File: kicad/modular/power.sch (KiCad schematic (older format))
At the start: 25 parts

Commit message: removed signal shield from power module, updated page settings
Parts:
- removed J?: SignalShield, symbol Connector_Shield:Shield_2x1x6
- J?: value PowerShield -> POWER
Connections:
- no-connect marks 6 -> 0
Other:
- note removed: "SIGNAL"
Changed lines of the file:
@@
 encoding utf-8
 Sheet 2 3
-Title ""
-Date ""
+Title "Position-sensitive detector (Power)"
+Date "2019-07-30"
 Rev ""
-Comp ""
-Comment1 ""
+Comp "Max Planck Institute of Quantum Optics"
+Comment1 "Bodo Kaiser"
 Comment2 ""
 Comment3 ""
@@
 U 1 1 5D4E31E6
 P 2000 2850
+AR Path="/5D4E31E6" Ref="J?"  Part="1"
+AR Path="/5D4C5F00/5D4E31E6" Ref="J?"  Part="1"
 F 0 "J?" H 1918 2525 50  0000 C CNN
 F 1 "CONN_PWR" H 1918 2616 50  0000 C CNN
@@
 U 1 1 5D4E31EC
 P 2750 2500
+AR Path="/5D4E31EC" Ref="#PWR?"  Part="1"
+AR Path="/5D4C5F00/5D4E31EC" Ref="#PWR?"  Part="1"
 F 0 "#PWR?" H 2750 2350 50  0001 C CNN
 F 1 "+15V" V 2765 2628 50  0000 L CNN
@@
 U 1 1 5D4E31F3
 P 2750 3200
+AR Path="/5D4E31F3" Ref="#PWR?"  Part="1"
+AR Path="/5D4C5F00/5D4E31F3" Ref="#PWR?"  Part="1"
 F 0 "#PWR?" H 2750 3300 50  0001 C CNN
 F 1 "-15V" V 2765 3328 50  0000 L CNN
@@
 U 1 1 5D4E31FB
 P 2750 2850
+AR Path="/5D4E31FB" Ref="#PWR?"  Part="1"
+AR Path="/5D4C5F00/5D4E31FB" Ref="#PWR?"  Part="1"
 F 0 "#PWR?" H 2750 2600 50  0001 C CNN
 F 1 "GND" V 2755 2722 50  0000 R CNN
@@
 U 1 1 5D4E3203
 P 2600 2450
+AR Path="/5D4E3203" Ref="#FLG?"  Part="1"
+AR Path="/5D4C5F00/5D4E3203" Ref="#FLG?"  Part="1"
 F 0 "#FLG?" H 2600 2525 50  0001 C CNN
 F 1 "PWR_FLAG" H 2600 2623 50  0000 C CNN
@@
 U 1 1 5D4E320C
 P 2600 2800
+AR Path="/5D4E320C" Ref="#FLG?"  Part="1"
+AR Path="/5D4C5F00/5D4E320C" Ref="#FLG?"  Part="1"
 F 0 "#FLG?" H 2600 2875 50  0001 C CNN
 F 1 "PWR_FLAG" H 2600 2973 50  0000 C CNN
@@
 U 1 1 5D4E3215
 P 2600 3150
+AR Path="/5D4E3215" Ref="#FLG?"  Part="1"
+AR Path="/5D4C5F00/5D4E3215" Ref="#FLG?"  Part="1"
 F 0 "#FLG?" H 2600 3225 50  0001 C CNN
 F 1 "PWR_FLAG" H 2600 3323 50  0000 C CNN
@@
 U 1 1 5D4E3225
 P 4950 2900
+AR Path="/5D4E3225" Ref="U?"  Part="1"
+AR Path="/5D4C5F00/5D4E3225" Ref="U?"  Part="1"
 F 0 "U?" H 4950 3142 50  0000 C CNN
 F 1 "LM317" H 4950 3051 50  0000 C CNN
@@
 U 1 1 5D4E322B
 P 3950 2900
+AR Path="/5D4E322B" Ref="#PWR?"  Part="1"
+AR Path="/5D4C5F00/5D4E322B" Ref="#PWR?"  Part="1"
 F 0 "#PWR?" H 3950 2750 50  0001 C CNN
 F 1 "+15V" V 3965 3028 50  0000 L CNN
@@
 U 1 1 5D4E323A
 P 4950 2450
+AR Path="/5D4E323A" Ref="D?"  Part="1"
+AR Path="/5D4C5F00/5D4E323A" Ref="D?"  Part="1"
 F 0 "D?" H 4950 2666 50  0000 C CNN
 F 1 "S1A" H 4950 2575 50  0000 C CNN
@@
 U 1 1 5D4E3241
 P 5450 3150
+AR Path="/5D4E3241" Ref="R?"  Part="1"
+AR Path="/5D4C5F00/5D4E3241" Ref="R?"  Part="1"
 F 0 "R?" H 5520 3196 50  0000 L CNN
 F 1 "120" H 5520 3105 50  0000 L CNN
@@
 U 1 1 5D4E3248
 P 3900 3900
+AR Path="/5D4E3248" Ref="#PWR?"  Part="1"
+AR Path="/5D4C5F00/5D4E3248" Ref="#PWR?"  Part="1"
 F 0 "#PWR?" H 3900 3650 50  0001 C CNN
 F 1 "GND" V 3905 3772 50  0000 R CNN
@@
 U 1 1 5D4E3253
 P 5450 3650
+AR Path="/5D4E3253" Ref="R?"  Part="1"
+AR Path="/5D4C5F00/5D4E3253" Ref="R?"  Part="1"
 F 0 "R?" H 5520 3696 50  0000 L CNN
 F 1 "1k" H 5520 3605 50  0000 L CNN
@@
 U 1 1 5D4E325C
 P 4100 2850
+AR Path="/5D4E325C" Ref="TP?"  Part="1"
+AR Path="/5D4C5F00/5D4E325C" Ref="TP?"  Part="1"
 F 0 "TP?" H 4050 3200 50  0000 L CNN
 F 1 "+15V" H 4000 3100 50  0000 L CNN
@@
 U 1 1 5D4E3266
 P 4450 3650
+AR Path="/5D4E3266" Ref="C?"  Part="1"
+AR Path="/5D4C5F00/5D4E3266" Ref="C?"  Part="1"
 F 0 "C?" H 4565 3696 50  0000 L CNN
 F 1 "100n" H 4565 3605 50  0000 L CNN
@@
 U 1 1 5D4E3274
 P 6000 3150
+AR Path="/5D4E3274" Ref="D?"  Part="1"
+AR Path="/5D4C5F00/5D4E3274" Ref="D?"  Part="1"
 F 0 "D?" V 5954 3229 50  0000 L CNN
 F 1 "S1A" V 6045 3229 50  0000 L CNN
@@
 U 1 1 5D4E327B
 P 6000 3650
+AR Path="/5D4E327B" Ref="C?"  Part="1"
+AR Path="/5D4C5F00/5D4E327B" Ref="C?"  Part="1"
 F 0 "C?" H 6115 3696 50  0000 L CNN
 F 1 "10u" H 6115 3605 50  0000 L CNN
@@
 U 1 1 5D4E3287
 P 6550 3150
+AR Path="/5D4E3287" Ref="C?"  Part="1"
+AR Path="/5D4C5F00/5D4E3287" Ref="C?"  Part="1"
 F 0 "C?" H 6665 3196 50  0000 L CNN
 F 1 "1u" H 6665 3105 50  0000 L CNN
@@
 U 1 1 5D4E328E
 P 7100 2900
+AR Path="/5D4E328E" Ref="#PWR?"  Part="1"
+AR Path="/5D4C5F00/5D4E328E" Ref="#PWR?"  Part="1"
 F 0 "#PWR?" H 7100 2750 50  0001 C CNN
 F 1 "+12V" V 7115 3028 50  0000 L CNN
@@
 U 1 1 5D4E3295
 P 4100 3850
+AR Path="/5D4E3295" Ref="TP?"  Part="1"
+AR Path="/5D4C5F00/5D4E3295" Ref="TP?"  Part="1"
 F 0 "TP?" H 4050 4200 50  0000 L CNN
 F 1 "GND" H 4050 4100 50  0000 L CNN
@@
 U 1 1 5D4E329E
 P 6900 2850
+AR Path="/5D4E329E" Ref="TP?"  Part="1"
+AR Path="/5D4C5F00/5D4E329E" Ref="TP?"  Part="1"
 F 0 "TP?" H 6850 3200 50  0000 L CNN
 F 1 "+12V" H 6800 3100 50  0000 L CNN
@@
 U 1 1 5D4E32A8
 P 4950 4900
+AR Path="/5D4E32A8" Ref="U?"  Part="1"
+AR Path="/5D4C5F00/5D4E32A8" Ref="U?"  Part="1"
 F 0 "U?" H 4950 4751 50  0000 C CNN
 F 1 "LM337" H 4950 4660 50  0000 C CNN
@@
 U 1 1 5D4E32AF
 P 4450 4150
+AR Path="/5D4E32AF" Ref="C?"  Part="1"
+AR Path="/5D4C5F00/5D4E32AF" Ref="C?"  Part="1"
 F 0 "C?" H 4565 4196 50  0000 L CNN
 F 1 "100n" H 4565 4105 50  0000 L CNN
@@
 U 1 1 5D4E32C5
 P 6550 4150
+AR Path="/5D4E32C5" Ref="C?"  Part="1"
+AR Path="/5D4C5F00/5D4E32C5" Ref="C?"  Part="1"
 F 0 "C?" H 6665 4196 50  0000 L CNN
 F 1 "1u" H 6665 4105 50  0000 L CNN
@@
 U 1 1 5D4E32CC
 P 6000 4650
+AR Path="/5D4E32CC" Ref="D?"  Part="1"
+AR Path="/5D4C5F00/5D4E32CC" Ref="D?"  Part="1"
 F 0 "D?" V 5954 4729 50  0000 L CNN
 F 1 "S1A" V 6045 4729 50  0000 L CNN
@@
 U 1 1 5D4E32D3
 P 6000 4150
+AR Path="/5D4E32D3" Ref="C?"  Part="1"
+AR Path="/5D4C5F00/5D4E32D3" Ref="C?"  Part="1"
 F 0 "C?" H 6115 4196 50  0000 L CNN
 F 1 "10u" H 6115 4105 50  0000 L CNN
@@
 U 1 1 5D4E32DA
 P 5450 4150
+AR Path="/5D4E32DA" Ref="R?"  Part="1"
+AR Path="/5D4C5F00/5D4E32DA" Ref="R?"  Part="1"
 F 0 "R?" H 5520 4196 50  0000 L CNN
 F 1 "1k" H 5520 4105 50  0000 L CNN
@@
 U 1 1 5D4E32E1
 P 5450 4650
+AR Path="/5D4E32E1" Ref="R?"  Part="1"
+AR Path="/5D4C5F00/5D4E32E1" Ref="R?"  Part="1"
 F 0 "R?" H 5520 4696 50  0000 L CNN
 F 1 "120" H 5520 4605 50  0000 L CNN
@@
 U 1 1 5D4E32EA
 P 4950 5350
+AR Path="/5D4E32EA" Ref="D?"  Part="1"
+AR Path="/5D4C5F00/5D4E32EA" Ref="D?"  Part="1"
 F 0 "D?" H 4950 5566 50  0000 C CNN
 F 1 "S1A" H 4950 5475 50  0000 C CNN
@@
 U 1 1 5D4E32F5
 P 4100 4850
+AR Path="/5D4E32F5" Ref="TP?"  Part="1"
+AR Path="/5D4C5F00/5D4E32F5" Ref="TP?"  Part="1"
 F 0 "TP?" H 4050 5200 50  0000 L CNN
 F 1 "-15V" H 4000 5100 50  0000 L CNN
@@
 U 1 1 5D4E32FE
 P 3900 4900
+AR Path="/5D4E32FE" Ref="#PWR?"  Part="1"
+AR Path="/5D4C5F00/5D4E32FE" Ref="#PWR?"  Part="1"
 F 0 "#PWR?" H 3900 5000 50  0001 C CNN
 F 1 "-15V" V 3915 5028 50  0000 L CNN
@@
 U 1 1 5D4E3305
 P 6900 4850
+AR Path="/5D4E3305" Ref="TP?"  Part="1"
+AR Path="/5D4C5F00/5D4E3305" Ref="TP?"  Part="1"
 F 0 "TP?" H 6850 5200 50  0000 L CNN
 F 1 "-12V" H 6800 5100 50  0000 L CNN
@@
 U 1 1 5D4E3310
 P 7100 4900
+AR Path="/5D4E3310" Ref="#PWR?"  Part="1"
+AR Path="/5D4C5F00/5D4E3310" Ref="#PWR?"  Part="1"
 F 0 "#PWR?" H 7100 5000 50  0001 C CNN
 F 1 "-12V" V 7115 5028 50  0000 L CNN
@@
 U 1 1 5D4E3316
 P 7100 3900
+AR Path="/5D4E3316" Ref="#PWR?"  Part="1"
+AR Path="/5D4C5F00/5D4E3316" Ref="#PWR?"  Part="1"
 F 0 "#PWR?" H 7100 3650 50  0001 C CNN
 F 1 "GND" V 7105 3772 50  0000 R CNN
@@
 U 1 1 5D4E3320
 P 6900 3850
+AR Path="/5D4E3320" Ref="TP?"  Part="1"
+AR Path="/5D4C5F00/5D4E3320" Ref="TP?"  Part="1"
 F 0 "TP?" H 6850 4200 50  0000 L CNN
 F 1 "GND" H 6850 4100 50  0000 L CNN
@@
 U 1 1 5D4E332B
 P 8600 2200
+AR Path="/5D4E332B" Ref="J?"  Part="1"
+AR Path="/5D4C5F00/5D4E332B" Ref="J?"  Part="1"
 F 0 "J?" H 8700 2150 50  0000 L CNN
-F 1 "PowerShield" H 8550 1000 50  0000 L CNN
+F 1 "POWER" H 8650 1000 50  0000 L CNN
 F 2 "" H 8600 2200 50  0001 C CNN
 F 3 "" H 8600 2200 50  0001 C CNN
@@
 U 1 1 5D4E3331
 P 8250 2600
+AR Path="/5D4E3331" Ref="#PWR?"  Part="1"
+AR Path="/5D4C5F00/5D4E3331" Ref="#PWR?"  Part="1"
 F 0 "#PWR?" H 8250 2450 50  0001 C CNN
 F 1 "+12V" V 8265 2728 50  0000 L CNN
@@
 U 1 1 5D4E3338
 P 8250 2750
+AR Path="/5D4E3338" Ref="#PWR?"  Part="1"
+AR Path="/5D4C5F00/5D4E3338" Ref="#PWR?"  Part="1"
 F 0 "#PWR?" H 8250 2500 50  0001 C CNN
 F 1 "GND" V 8255 2622 50  0000 R CNN
@@
 U 1 1 5D4E3343
 P 8250 3050
+AR Path="/5D4E3343" Ref="#PWR?"  Part="1"
+AR Path="/5D4C5F00/5D4E3343" Ref="#PWR?"  Part="1"
 F 0 "#PWR?" H 8250 3150 50  0001 C CNN
 F 1 "-12V" V 8265 3178 50  0000 L CNN
@@
 U 1 1 5D4E334A
 P 8250 2450
+AR Path="/5D4E334A" Ref="#PWR?"  Part="1"
+AR Path="/5D4C5F00/5D4E334A" Ref="#PWR?"  Part="1"
 F 0 "#PWR?" H 8250 2300 50  0001 C CNN
 F 1 "+15V" V 8265 2578 50  0000 L CNN
@@
 U 1 1 5D4E3350
 P 8250 3200
+AR Path="/5D4E3350" Ref="#PWR?"  Part="1"
+AR Path="/5D4C5F00/5D4E3350" Ref="#PWR?"  Part="1"
 F 0 "#PWR?" H 8250 3300 50  0001 C CNN
 F 1 "-15V" V 8265 3328 50  0000 L CNN
@@
 Text Notes 7850 2100 0    50   ~ 0
 POWER OUTPUT
-NoConn ~ 8500 4250
-NoConn ~ 8500 4400
-NoConn ~ 8500 4550
-NoConn ~ 8500 4700
-NoConn ~ 8500 4850
-NoConn ~ 8500 5000
-$Comp
-L Connector_Shield:Shield_2x1x6 J?
-U 2 1 5D4E3363
-P 8600 4000
-F 0 "J?" H 8700 3950 50  0000 L CNN
-F 1 "SignalShield" H 8550 2800 50  0000 L CNN
-F 2 "" H 8600 4000 50  0001 C CNN
-F 3 "" H 8600 4000 50  0001 C CNN
-	2    8600 4000
-	1    0    0    -1
-$EndComp
-Wire Notes Line
-	7850 3950 9250 3950
-Wire Notes Line
-	9250 3950 9250 5350
-Wire Notes Line
-	9250 5350 7850 5350
-Wire Notes Line
-	7850 5350 7850 3950
-Text Notes 7850 3900 0    50   ~ 0
-SIGNAL
 $EndSCHEMATC

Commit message: added more test points to modular, assigned some footprints
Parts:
- removed J?: POWER, symbol Connector_Shield:Shield_2x1x6
- added J2: HEADER_SIG, symbol Connector_Shield:Shield_2x1x6
- C1, C2, C3, C4, C5, C6: renamed from C?; footprint (none) -> Capacitor_SMD:C_0603_1608Metric
- D1, D2, D3, D4: renamed from D?; footprint (none) -> Diode_SMD:D_SMA
- J1: renamed from J?; footprint (none) -> TerminalBlock_TE-Connectivity:TerminalBlock_TE_282834-3_1x03_P2.54mm_Horizontal
- R1, R2, R3, R4: renamed from R?; footprint (none) -> Resistor_SMD:R_0603_1608Metric
- TP1, TP2, TP3, TP4, TP5, TP6: renamed from TP?; footprint (none) -> TestPoint:TestPoint_THTPad_D1.0mm_Drill0.5mm
- U1: renamed from U?; footprint (none) -> Package_TO_SOT_SMD:SOT-223-3_TabPin2
- gave numbers to parts that had none: 1
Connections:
- no-connect marks 0 -> 6

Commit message: completed header footprint, started with pcb design of power board
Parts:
- removed unit 2 of J2
- removed TP5: GND, TestPoint:TestPoint_THTPad_D1.0mm_Drill0.5mm, symbol Connector:TestPoint
- J2: value HEADER_SIG -> HEADER; footprint (none) -> Connector_Header:PinHeader_2.54mm; symbol Connector_Shield:Shield_2x1x6 -> Connector_Header:Header
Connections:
- wire segments 88 -> 86
- no-connect marks 6 -> 0
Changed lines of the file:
@@
 	0    -1   1    0
-$EndComp
-Wire Wire Line
-	7100 3900 6900 3900
-Wire Wire Line
-	6900 3850 6900 3900
-Connection ~ 6900 3900
-Wire Wire Line
-	6900 3900 6550 3900
-$Comp
-L Connector:TestPoint TP?
-U 1 1 5D4E3320
-P 6900 3850
-AR Path="/5D4E3320" Ref="TP?"  Part="1"
-AR Path="/5D4C5F00/5D4E3320" Ref="TP5"  Part="1"
-F 0 "TP5" H 6850 4200 50  0000 L CNN
-F 1 "GND" H 6850 4100 50  0000 L CNN
-F 2 "TestPoint:TestPoint_THTPad_D1.0mm_Drill0.5mm" H 7100 3850 50  0001 C CNN
-F 3 "~" H 7100 3850 50  0001 C CNN
-	1    6900 3850
-	1    0    0    -1
 $EndComp
 Wire Notes Line
@@
 POWER OUTPUT
 $Comp
-L Connector_Shield:Shield_2x1x6 J2
+L Connector_Header:Header J2
 U 1 1 5D7DD68E
 P 8600 2200
 F 0 "J2" H 8700 2150 50  0000 L CNN
-F 1 "HEADER_SIG" H 8550 1000 50  0000 L CNN
-F 2 "" H 8600 2200 50  0001 C CNN
+F 1 "HEADER" H 8550 1000 50  0000 L CNN
+F 2 "Connector_Header:PinHeader_2.54mm" H 8600 2200 50  0001 C CNN
 F 3 "" H 8600 2200 50  0001 C CNN
 	1    8600 2200
 	1    0    0    -1
 $EndComp
-$Comp
-L Connector_Shield:Shield_2x1x6 J2
-U 2 1 5D7DEA95
-P 8600 4000
-F 0 "J2" H 8700 3950 50  0000 L CNN
-F 1 "HEADER_SIG" H 8550 2800 50  0000 L CNN
-F 2 "" H 8600 4000 50  0001 C CNN
-F 3 "" H 8600 4000 50  0001 C CNN
-	2    8600 4000
-	1    0    0    -1
-$EndComp
-NoConn ~ 8500 4250
-NoConn ~ 8500 4400
-NoConn ~ 8500 4550
-NoConn ~ 8500 4700
-NoConn ~ 8500 4850
-NoConn ~ 8500 5000
+Wire Wire Line
+	6550 3900 7100 3900
 $EndSCHEMATC

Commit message: started redesign of pcb
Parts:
- removed TP1: +15V, TestPoint:TestPoint_THTPad_D1.0mm_Drill0.5mm, symbol Connector:TestPoint
- removed TP2: GND, TestPoint:TestPoint_THTPad_D1.0mm_Drill0.5mm, symbol Connector:TestPoint
- removed TP3: -15V, TestPoint:TestPoint_THTPad_D1.0mm_Drill0.5mm, symbol Connector:TestPoint
- removed TP4: +12V, TestPoint:TestPoint_THTPad_D1.0mm_Drill0.5mm, symbol Connector:TestPoint
- removed TP6: -12V, TestPoint:TestPoint_THTPad_D1.0mm_Drill0.5mm, symbol Connector:TestPoint
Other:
- moved on the sheet: C1, C2, C3, C4, C5, C6, D1, D2, D3, D4, J2A, R1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

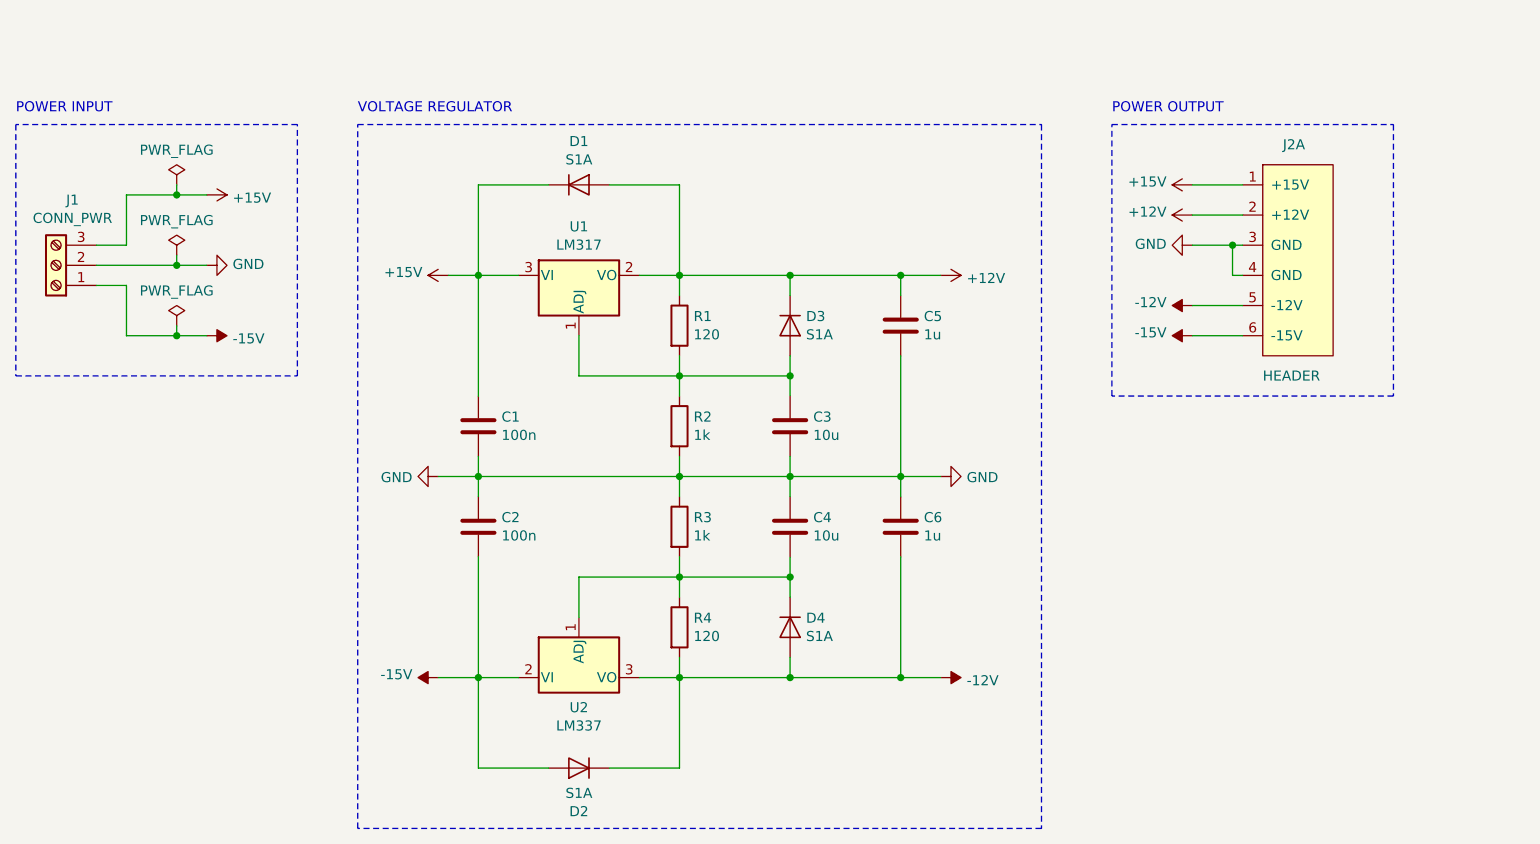
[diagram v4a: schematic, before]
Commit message: applied pcb design suggestions to modular boards
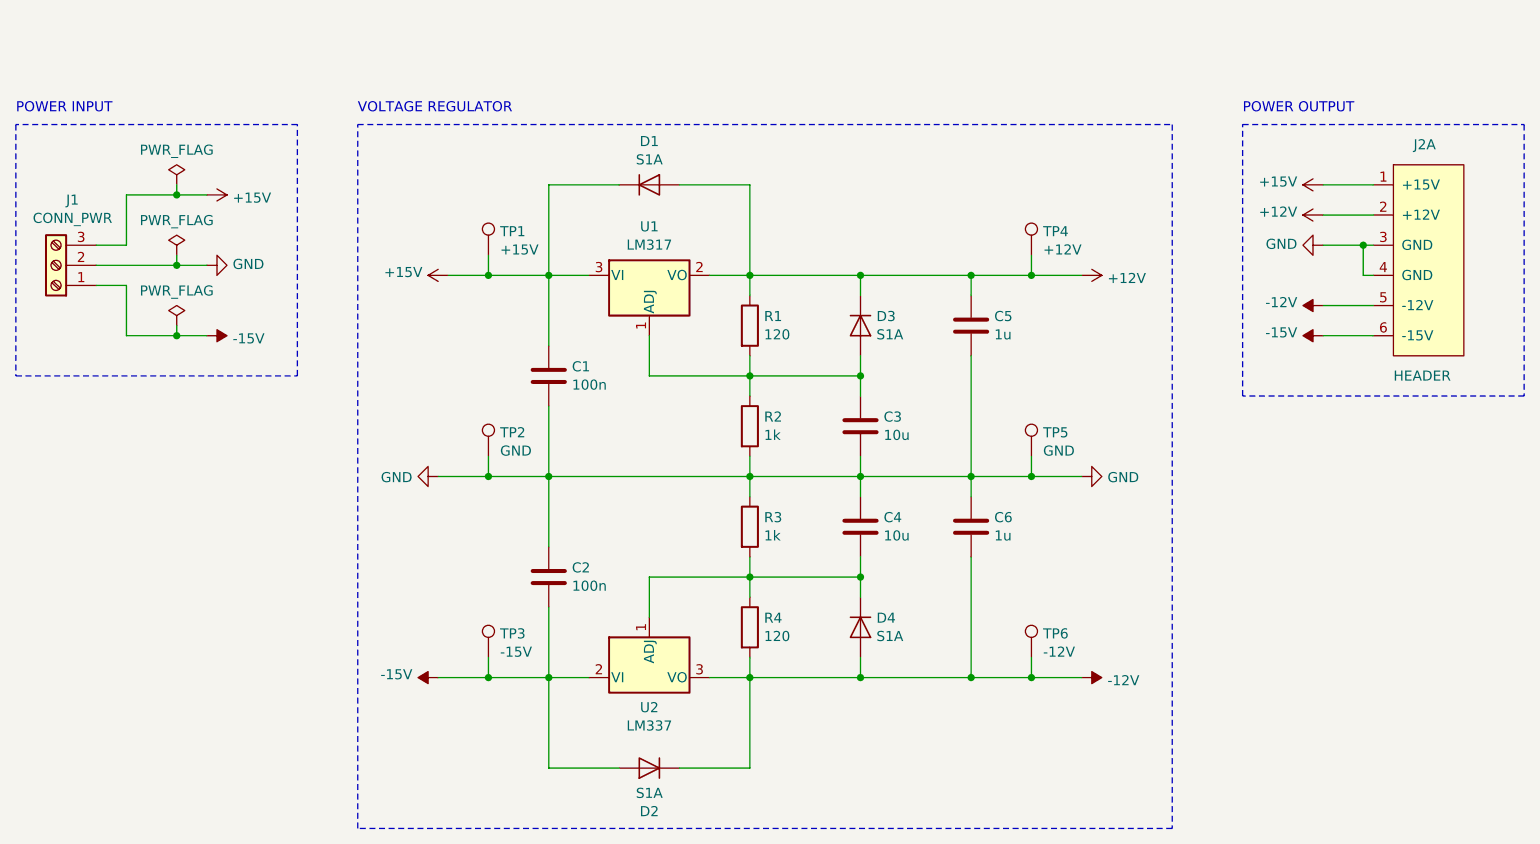
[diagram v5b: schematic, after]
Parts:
- added TP1: +15V, TestPoint:TestPoint_THTPad_D1.0mm_Drill0.5mm, symbol Connector:TestPoint
- added TP2, TP5: GND, TestPoint:TestPoint_THTPad_D1.0mm_Drill0.5mm, symbol Connector:TestPoint
- added TP3: -15V, TestPoint:TestPoint_THTPad_D1.0mm_Drill0.5mm, symbol Connector:TestPoint
- added TP4: +12V, TestPoint:TestPoint_THTPad_D1.0mm_Drill0.5mm, symbol Connector:TestPoint
- added TP6: -12V, TestPoint:TestPoint_THTPad_D1.0mm_Drill0.5mm, symbol Connector:TestPoint
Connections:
- net +12V: now also TP4.1
- net +15V: now also TP1.1
- net -12V: now also TP6.1
- net -15V: now also TP3.1
- net GND: now also TP2.1, TP5.1
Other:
- moved on the sheet: C1, C2, C3, C4, C5, C6, D1, D2, D3, D4, J2A, R1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
